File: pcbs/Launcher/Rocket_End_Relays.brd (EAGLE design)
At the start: 40 parts, among them IC2 LM2576T-ADJ, K4 LD105, K5 LD105, K6 LD105, K7 LD105, T1 BC547, T2 BC547, T3 BC547, T4 BC547, T5 BC547, U1 ARDUINO-MEGAPRO-5V, X1 1751248, X2 22-23-2041, X3 22-23-2021, X4 1751248, X5 22-23-2021

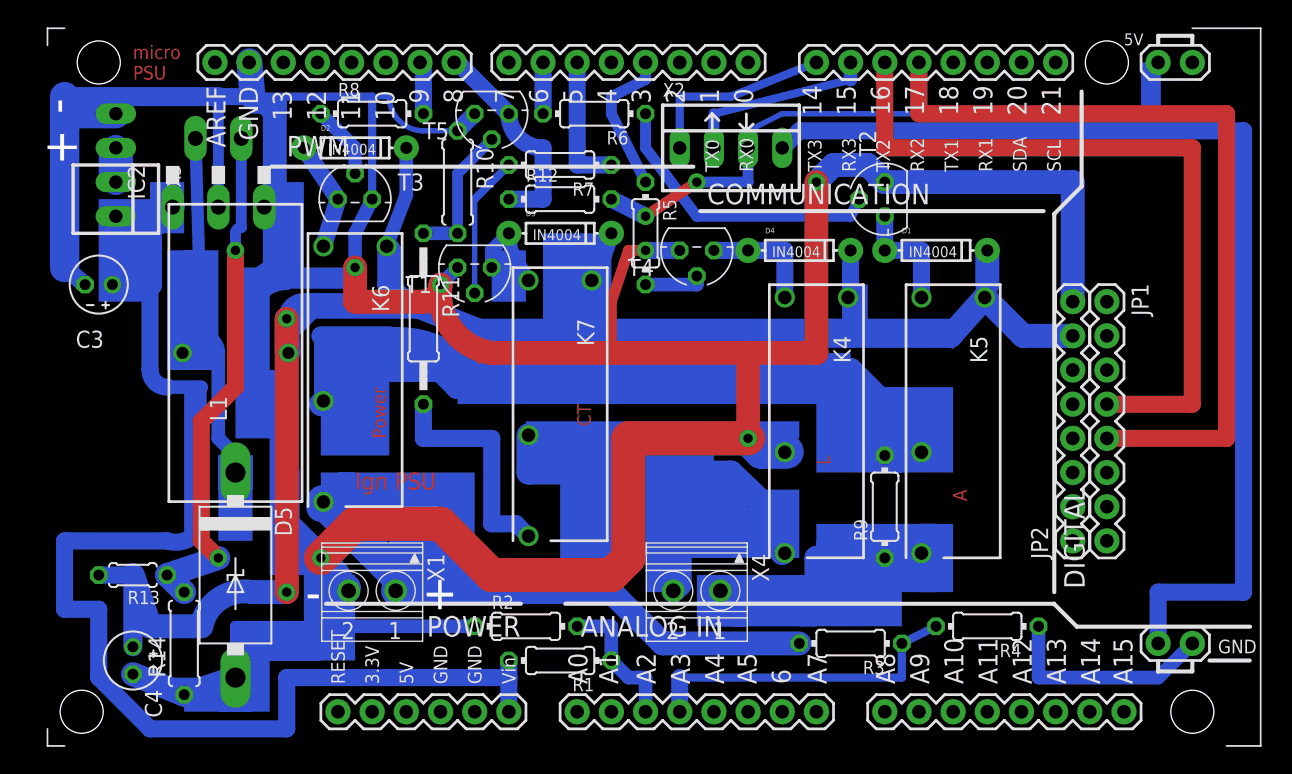
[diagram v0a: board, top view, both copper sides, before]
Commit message: * Moving relays in line a bit more * Added additional connector for Igniter battery, to give us more options * Rotated plugs
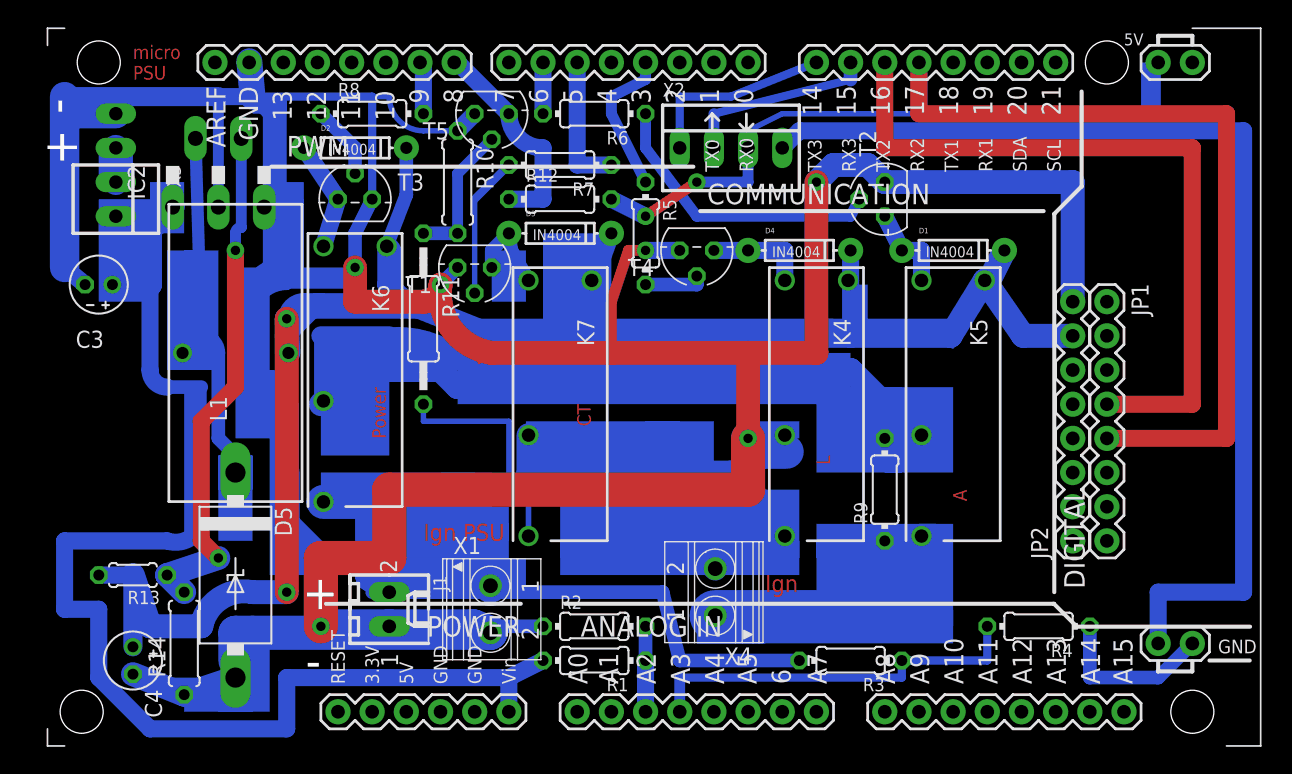
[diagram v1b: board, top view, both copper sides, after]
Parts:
- added J1: 22-27-2021-02, con-molex:6410-02
- moved X1 8.98 mm to (36.8, 17.8), turned to 270 degrees
- moved R2 5.08 mm to (44.5, 16.5)
- moved R4 3.81 mm to (77.5, 16.5)
- moved R1 2.54 mm to (44.5, 14.0)
- moved D1 1.27 mm to (71.1, 44.5)
- moved K4 1.27 mm to (61.0, 33.0)
- moved K5 1.27 mm to (71.1, 33.0)
- moved R9 1.27 mm to (66.0, 26.7)
- moved X4 1.27 mm to (53.3, 19.1), turned to 90 degrees
- moved R3 1.27 mm to (63.5, 14.0)
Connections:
- net N$29: now also J1.2
- net N$33: now also J1.1
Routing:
- net N$33: track 313.8 -> 341.3 mm
- net N$25: track 0.00 -> 8.89 mm
- net N$29: track 40.9 -> 45.7 mm
- net N$3: track 24.4 -> 29.2 mm
- net N$17: track 18.2 -> 22.6 mm
- net N$7: track 10.7 -> 6.35 mm
- net N$24: track 16.3 -> 12.5 mm
- net N$22: track 8.77 -> 6.53 mm
- net N$5: track 159.9 -> 161.5 mm
- net N$15: track 39.3 -> 40.9 mm
- net VCC: track 97.2 -> 98.8 mm
- net N$19: track 8.77 -> 7.50 mm
- net N$30: track 17.1 -> 17.6 mm
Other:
- board text added: "Ign"

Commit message: * Moving Other serial port connector (for stills) near to RFD900 connectors so we don't run into issues with width being exceeded and wires being bent/cramped.
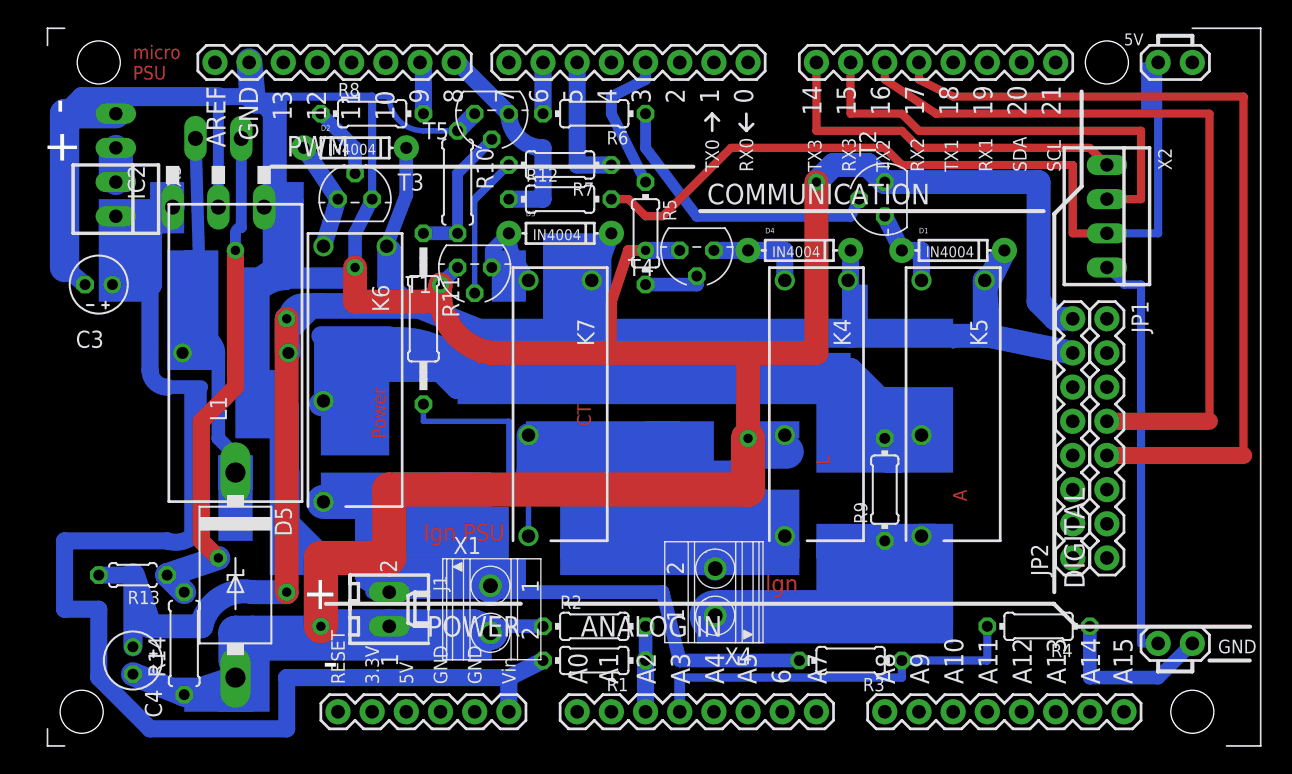
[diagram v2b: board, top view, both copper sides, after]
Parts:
- moved X2 28.4 mm to (82.5, 47.0), turned to 270 degrees
- moved JP1 1.27 mm to (82.5, 39.4)
- moved JP2 1.27 mm to (80.0, 21.6)
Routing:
- net N$16: track 79.7 -> 31.0 mm
- net N$27: track 14.3 -> 33.5 mm
- net N$6: track 14.5 -> 27.7 mm
- net N$23: track 49.6 -> 61.6 mm, vias 2 -> 0
- net N$5: track 161.5 -> 168.1 mm
- net N$2: track 59.7 -> 62.5 mm
- net N$1: track 54.6 -> 56.6 mm

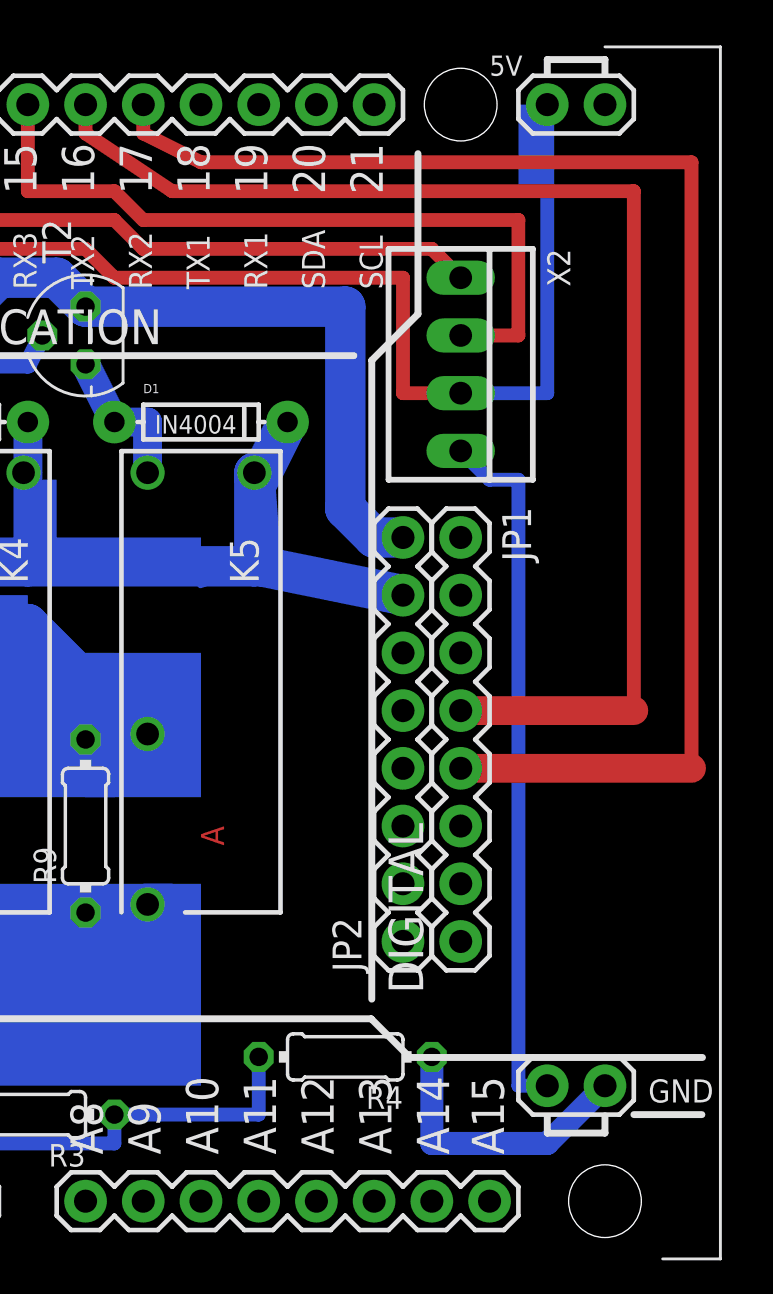
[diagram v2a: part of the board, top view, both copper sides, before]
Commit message: * More refinements to tracks. Trying to avoid edge of board.
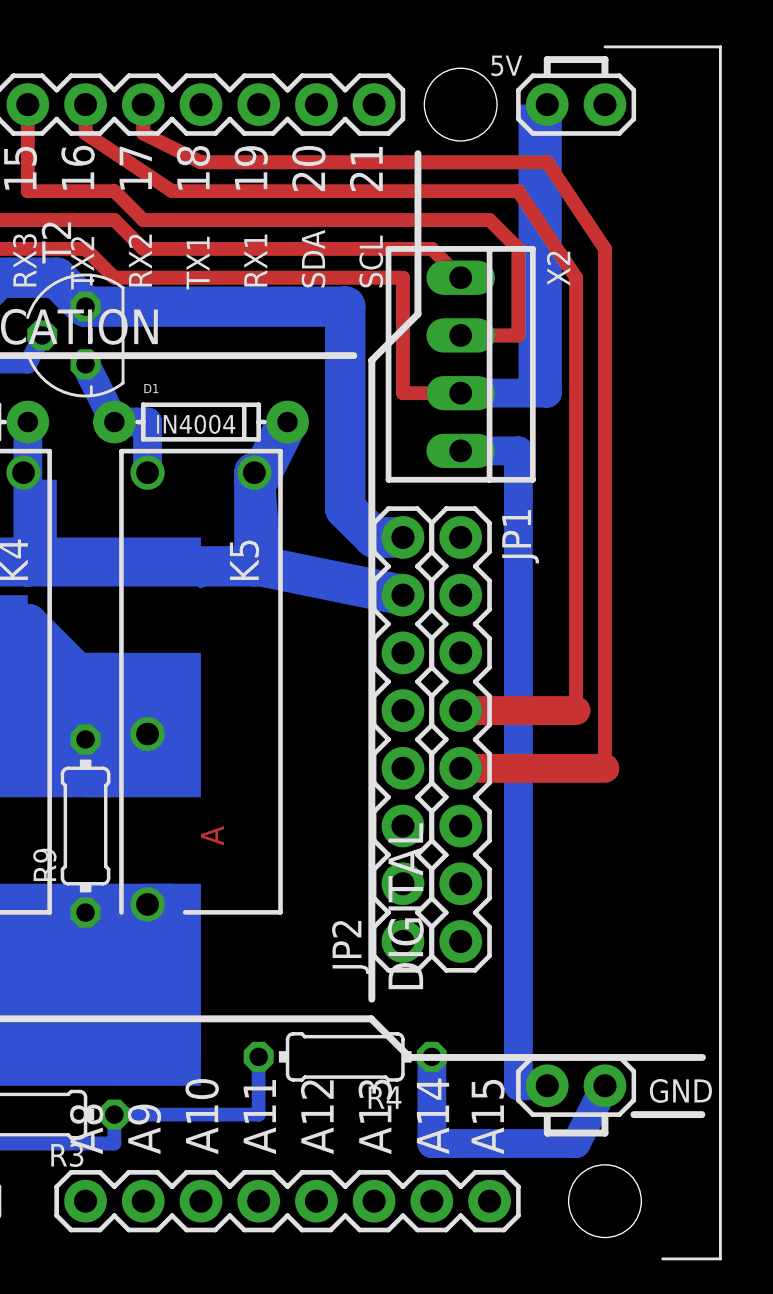
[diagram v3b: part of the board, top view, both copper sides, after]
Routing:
- net N$2: track 62.5 -> 53.1 mm
- net N$1: track 56.6 -> 49.8 mm
- net N$27: track 33.5 -> 32.8 mm
- net N$16: track 31.0 -> 31.8 mm
- net N$24: track 12.5 -> 13.0 mm
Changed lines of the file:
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@@
 <rectangle x1="36.83" y1="40.64" x2="39.37" y2="41.91" layer="16"/>
 <rectangle x1="19.05" y1="54.61" x2="21.59" y2="55.88" layer="16"/>
-<rectangle x1="85.09" y1="54.61" x2="86.36" y2="58.42" layer="16"/>
 <rectangle x1="17.78" y1="31.75" x2="19.05" y2="43.18" layer="16"/>
 <rectangle x1="19.05" y1="31.75" x2="20.32" y2="33.02" layer="16"/>
@@
 <rectangle x1="52.07" y1="15.24" x2="71.12" y2="17.78" layer="16"/>
 <rectangle x1="19.05" y1="13.97" x2="36.83" y2="15.24" layer="16"/>
+<rectangle x1="85.09" y1="45.72" x2="86.36" y2="58.42" layer="16"/>
 </plain>
 <attributes>
@@
 <wire x1="66.04" y1="57.15" x2="69.85" y2="54.61" width="0.6096" layer="1"/>
 <contactref element="JP1" pad="4"/>
-<wire x1="69.85" y1="54.61" x2="90.17" y2="54.61" width="0.6096" layer="1"/>
-<wire x1="90.17" y1="54.61" x2="90.17" y2="31.75" width="0.6096" layer="1"/>
-<wire x1="90.17" y1="31.75" x2="82.55" y2="31.75" width="1.27" layer="1"/>
+<wire x1="69.85" y1="54.61" x2="85.09" y2="54.61" width="0.6096" layer="1"/>
+<wire x1="85.09" y1="54.61" x2="87.63" y2="50.8" width="0.6096" layer="1"/>
+<wire x1="87.63" y1="50.8" x2="87.63" y2="31.75" width="0.6096" layer="1"/>
+<wire x1="87.63" y1="31.75" x2="82.55" y2="31.75" width="1.27" layer="1"/>
 </signal>
 <signal name="N$2">
@@
 <wire x1="68.58" y1="58.42" x2="68.58" y2="57.15" width="0.6096" layer="1"/>
 <wire x1="68.58" y1="57.15" x2="71.12" y2="55.88" width="0.6096" layer="1"/>
-<wire x1="71.12" y1="55.88" x2="92.71" y2="55.88" width="0.6096" layer="1"/>
-<wire x1="92.71" y1="55.88" x2="92.71" y2="29.21" width="0.6096" layer="1"/>
+<wire x1="71.12" y1="55.88" x2="86.36" y2="55.88" width="0.6096" layer="1"/>
+<wire x1="86.36" y1="55.88" x2="88.9" y2="52.07" width="0.6096" layer="1"/>
+<wire x1="88.9" y1="52.07" x2="88.9" y2="29.21" width="0.6096" layer="1"/>
 <contactref element="JP1" pad="5"/>
-<wire x1="92.71" y1="29.21" x2="82.55" y2="29.21" width="1.27" layer="1"/>
+<wire x1="88.9" y1="29.21" x2="82.55" y2="29.21" width="1.27" layer="1"/>
 </signal>
 <signal name="N$14">
@@
 <contactref element="X2" pad="2"/>
 <wire x1="82.55" y1="48.26" x2="85.09" y2="48.26" width="0.6096" layer="1"/>
-<wire x1="85.09" y1="48.26" x2="85.09" y2="53.34" width="0.6096" layer="1"/>
-<wire x1="85.09" y1="53.34" x2="68.58" y2="53.34" width="0.6096" layer="1"/>
+<wire x1="85.09" y1="48.26" x2="85.09" y2="52.07" width="0.6096" layer="1"/>
+<wire x1="85.09" y1="52.07" x2="83.82" y2="53.34" width="0.6096" layer="1"/>
+<wire x1="83.82" y1="53.34" x2="68.58" y2="53.34" width="0.6096" layer="1"/>
 <wire x1="68.58" y1="53.34" x2="67.31" y2="54.61" width="0.6096" layer="1"/>
 <wire x1="67.31" y1="54.61" x2="63.5" y2="54.61" width="0.6096" layer="1"/>
@@
 <contactref element="X2" pad="4"/>
 <contactref element="U1" pad="GND@2"/>
-<wire x1="86.36" y1="15.24" x2="85.09" y2="15.24" width="0.6096" layer="16"/>
-<wire x1="85.09" y1="15.24" x2="85.09" y2="41.91" width="0.6096" layer="16"/>
-<wire x1="85.09" y1="41.91" x2="83.82" y2="41.91" width="0.6096" layer="16"/>
-<wire x1="83.82" y1="41.91" x2="82.55" y2="43.18" width="0.6096" layer="16"/>
+<wire x1="86.36" y1="15.24" x2="85.09" y2="15.24" width="1.27" layer="16"/>
+<wire x1="85.09" y1="15.24" x2="85.09" y2="43.18" width="1.27" layer="16"/>
+<wire x1="85.09" y1="43.18" x2="82.55" y2="43.18" width="1.27" layer="16"/>
 </signal>
 <signal name="N$24">
 <contactref element="R4" pad="1"/>
 <contactref element="U1" pad="GND@3"/>
-<wire x1="88.9" y1="15.24" x2="86.36" y2="12.7" width="1.016" layer="16"/>
-<wire x1="86.36" y1="12.7" x2="81.28" y2="12.7" width="1.016" layer="16"/>
-<wire x1="81.28" y1="12.7" x2="81.28" y2="16.51" width="1.016" layer="16"/>
+<wire x1="88.9" y1="15.24" x2="87.63" y2="12.7" width="1.27" layer="16"/>
+<wire x1="87.63" y1="12.7" x2="81.28" y2="12.7" width="1.27" layer="16"/>
+<wire x1="81.28" y1="12.7" x2="81.28" y2="16.51" width="1.27" layer="16"/>
 </signal>
 <signal name="N$37">
@@
 <wire x1="80.01" y1="50.8" x2="67.31" y2="50.8" width="0.6096" layer="1"/>
 <wire x1="67.31" y1="50.8" x2="66.04" y2="52.07" width="0.6096" layer="1"/>
-<wire x1="82.55" y1="45.72" x2="86.36" y2="45.72" width="0.6096" layer="16"/>
-<wire x1="86.36" y1="45.72" x2="86.36" y2="58.42" width="0.6096" layer="16"/>
+<wire x1="82.55" y1="45.72" x2="86.36" y2="45.72" width="1.27" layer="16"/>
+<wire x1="86.36" y1="45.72" x2="86.36" y2="58.42" width="1.27" layer="16"/>
 </signal>
 <signal name="N$18">

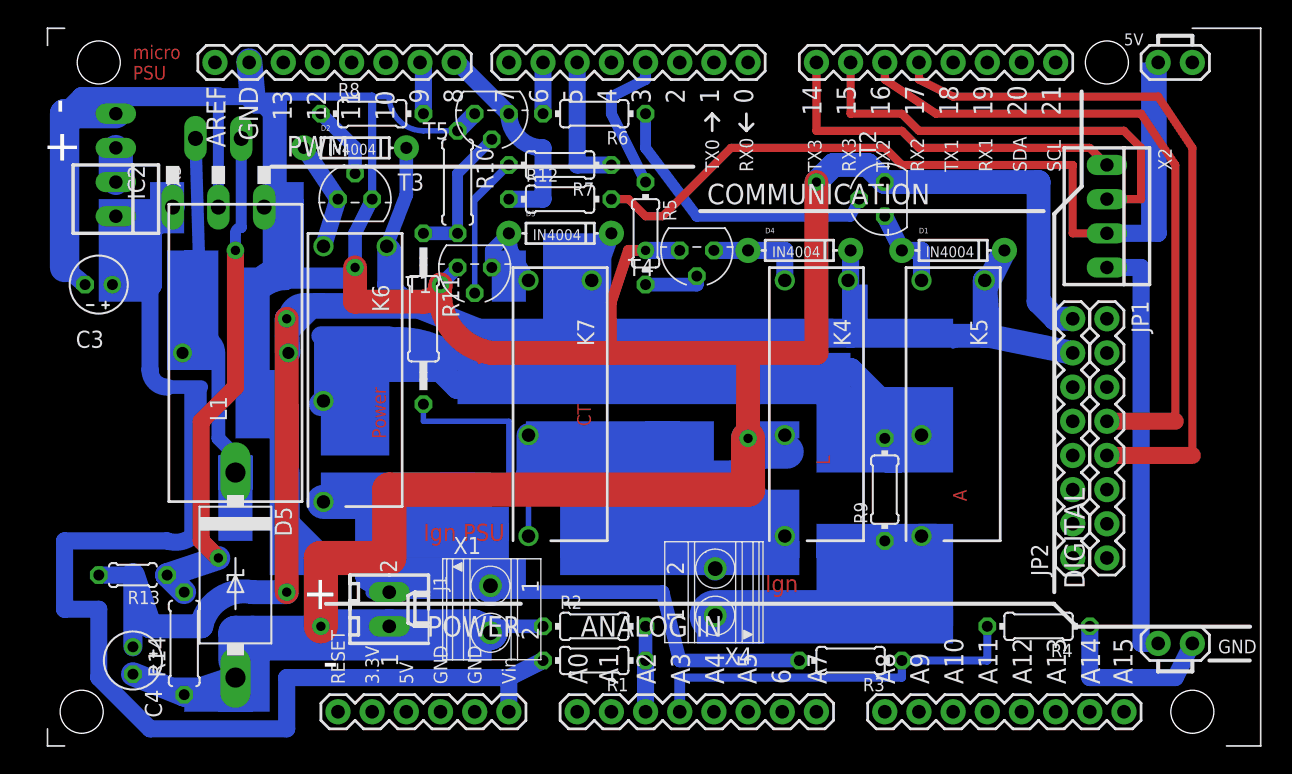
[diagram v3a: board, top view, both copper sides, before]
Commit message: * spacing out some of the components a little * moving the camera serial port connector back one step from edge of PCB.
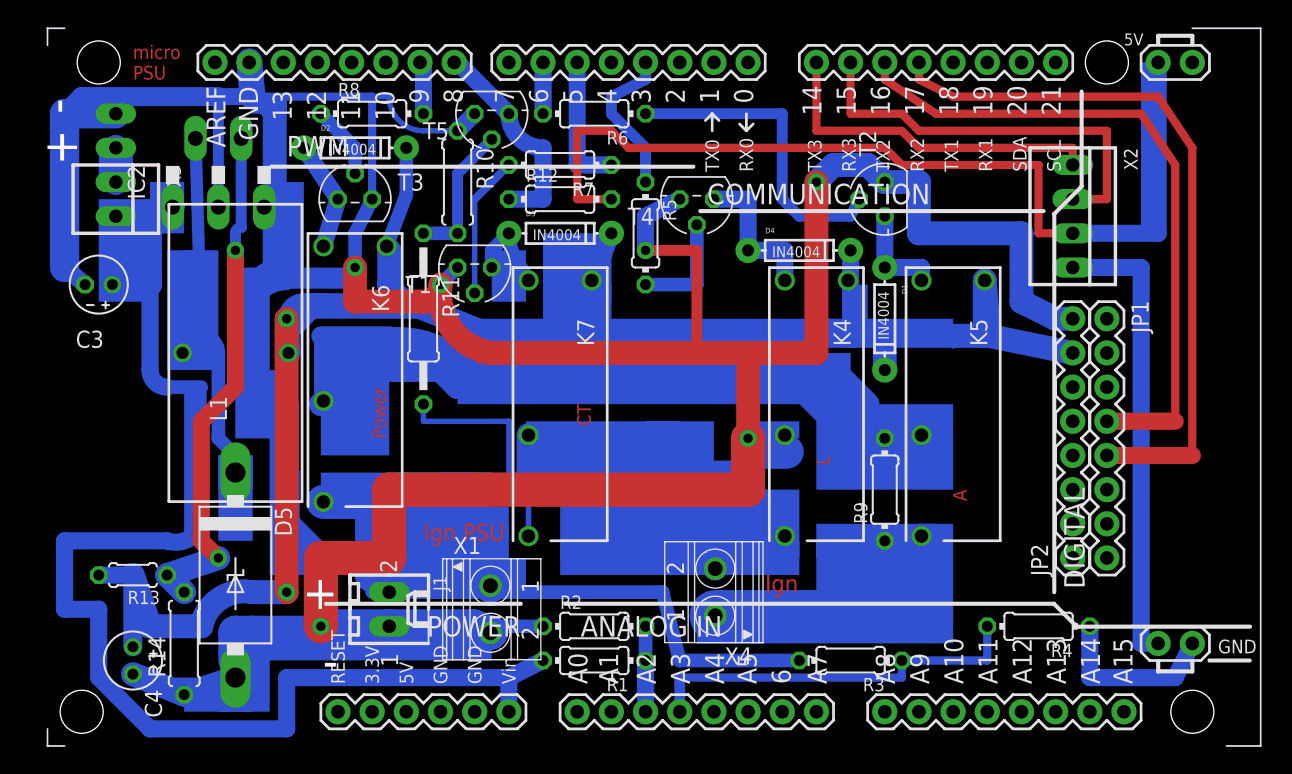
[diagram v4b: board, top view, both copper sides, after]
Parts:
- moved D1 7.18 mm to (66.0, 39.4), turned to 270 degrees
- moved T4 3.81 mm to (52.1, 48.3)
- moved X2 2.54 mm to (80.0, 47.0)
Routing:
- net N$23: track 61.6 -> 69.6 mm
- net N$34: track 0.00 -> 5.39 mm
- net N$33: track 341.0 -> 346.0 mm
- net N$19: track 7.50 -> 11.3 mm
- net N$12: track 4.45 -> 8.26 mm
- net N$35: track 0.00 -> 3.59 mm
- net N$16: track 31.8 -> 34.3 mm
- net N$27: track 32.8 -> 31.0 mm
- net N$10: track 21.7 -> 23.5 mm
- net N$6: track 27.7 -> 25.9 mm
- net N$28: track 81.6 -> 79.8 mm
- net N$22: track 6.53 -> 7.50 mm
